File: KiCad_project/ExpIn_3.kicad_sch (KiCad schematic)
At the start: 30 parts, among them J1 NMJ6HCD2, J2 Conn_01x08_MountingPin, J3 Conn_01x02_MountingPin, SW1 SW_Push, U1 74HC4066, U2 MCP6001-OT, U3 MCP4018T-103E/LT, U5 USBLC6-2SC6

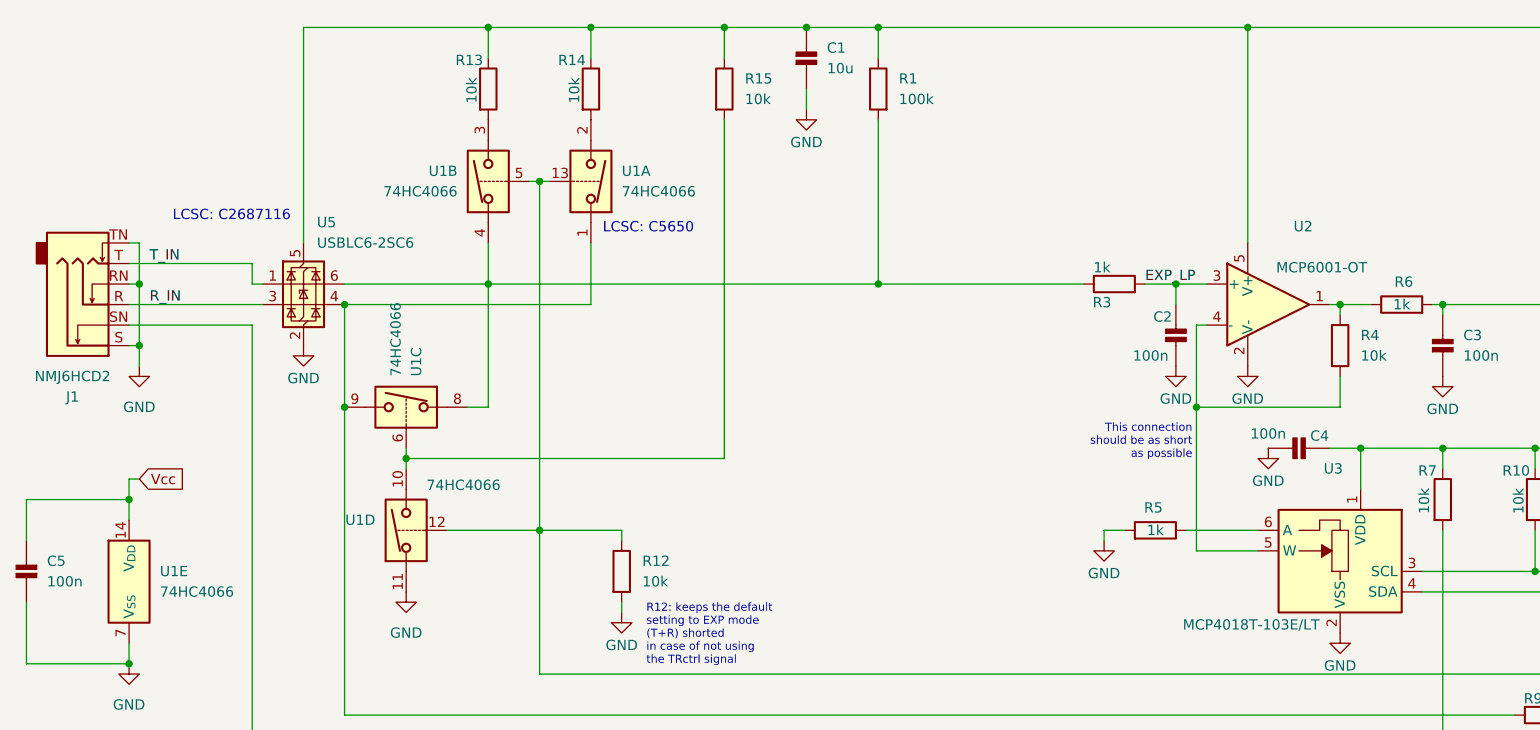
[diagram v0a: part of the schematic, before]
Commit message: SMT connectors, gain control
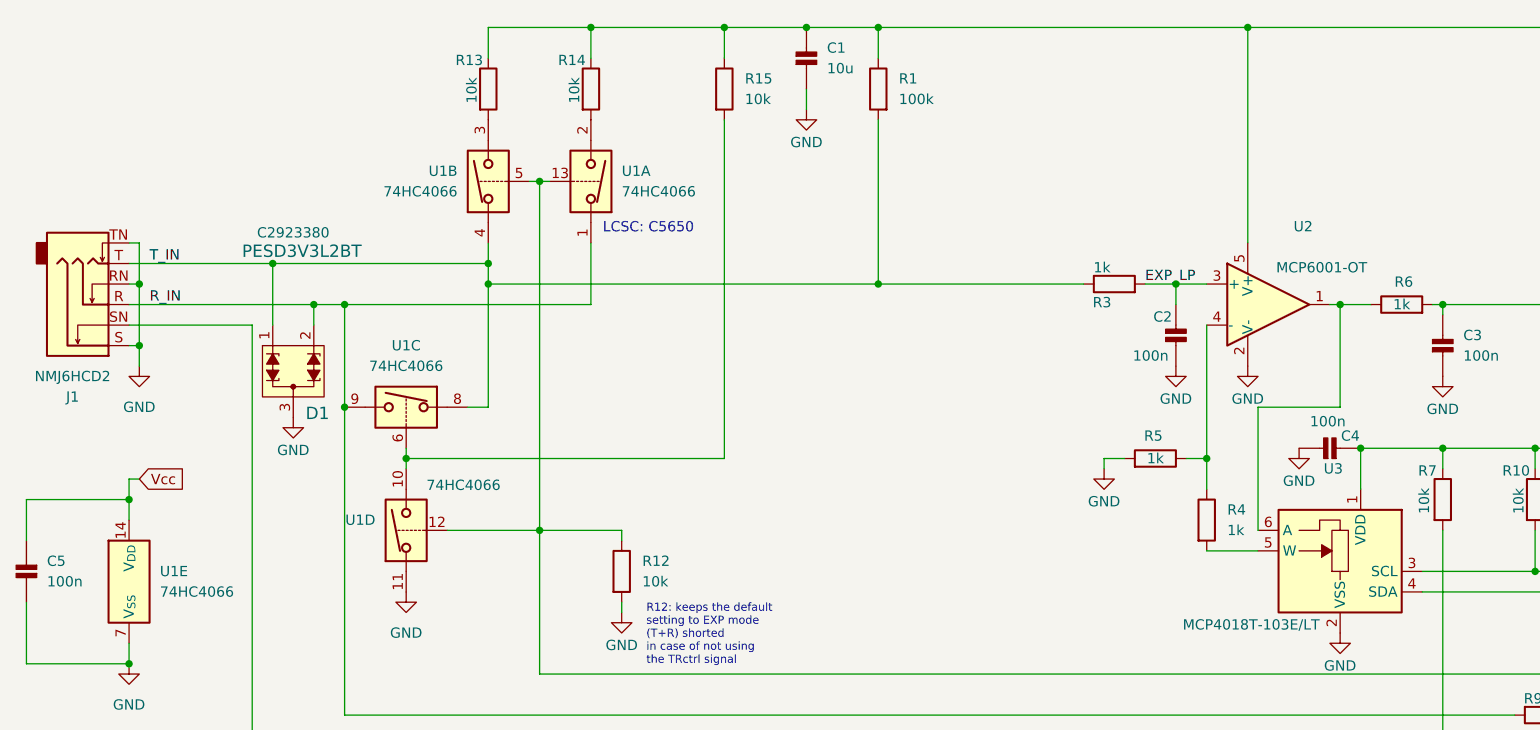
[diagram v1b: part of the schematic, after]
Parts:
- removed U5: USBLC6-2SC6, Package_TO_SOT_SMD:SOT-23-6, symbol Power_Protection:USBLC6-2SC6
- added D1: PESD3V3L2BT, H_SOT:SOT-23, symbol H_diodes:PESD5V0S2BT
- J2: footprint Connector_Molex:Molex_PicoBlade_53047-0810_1x08_P1.25mm_Vertical -> Connector_JST:JST_SH_BM08B-SRSS-TB_1x08-1MP_P1.00mm_Vertical
- J3: footprint Connector_Molex:Molex_PicoBlade_53047-0210_1x02_P1.25mm_Vertical -> Connector_JST:JST_PH_B2B-PH-SM4-TB_1x02-1MP_P2.00mm_Vertical
- R4: value 10k -> 1k
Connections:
- net GND: now also D1.3
- net R_IN: now also R9.2, U1.1, U1.9, D1.2
- net T_IN: now also R1.2, R3.1, U1.4, U1.8, D1.1
- net at R5.1: now also R4.1, U2.4 (-); no longer U3.6 (A)
- net at R6.1, U2.1: now also U3.6 (A); no longer R4.1
- net at R4.2, U3.5 (W): no longer U2.4 (-)
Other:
- note removed: "LCSC: C2687116"
- note removed: "This connection should be as short as possible"
- moved on the sheet: C4, R4, R5

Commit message: board size update, dec. caps 1u, bom
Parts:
- C1: value 10u -> 1u
- C4, C5: value 100n -> 1u
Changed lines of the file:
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@@
 			)
 		)
-		(property "Value" "100n"
+		(property "Value" "1u"
 			(at 180.086 65.278 90)
 			(effects
@@
 			)
 		)
-		(property "Value" "100n"
+		(property "Value" "1u"
 			(at 21.59 85.0899 0)
 			(effects
@@
 			)
 		)
-		(property "Value" "10u"
+		(property "Value" "1u"
 			(at 118.11 21.5899 0)
 			(effects
